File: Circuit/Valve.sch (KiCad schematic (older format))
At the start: 22 parts, among them CN1 GROVE, CN2 ST-LINK, CN3 TTL-232R-3V3, J1 Conn_01x04_Male, SW1 RESET, U1 STM32L010F4P6

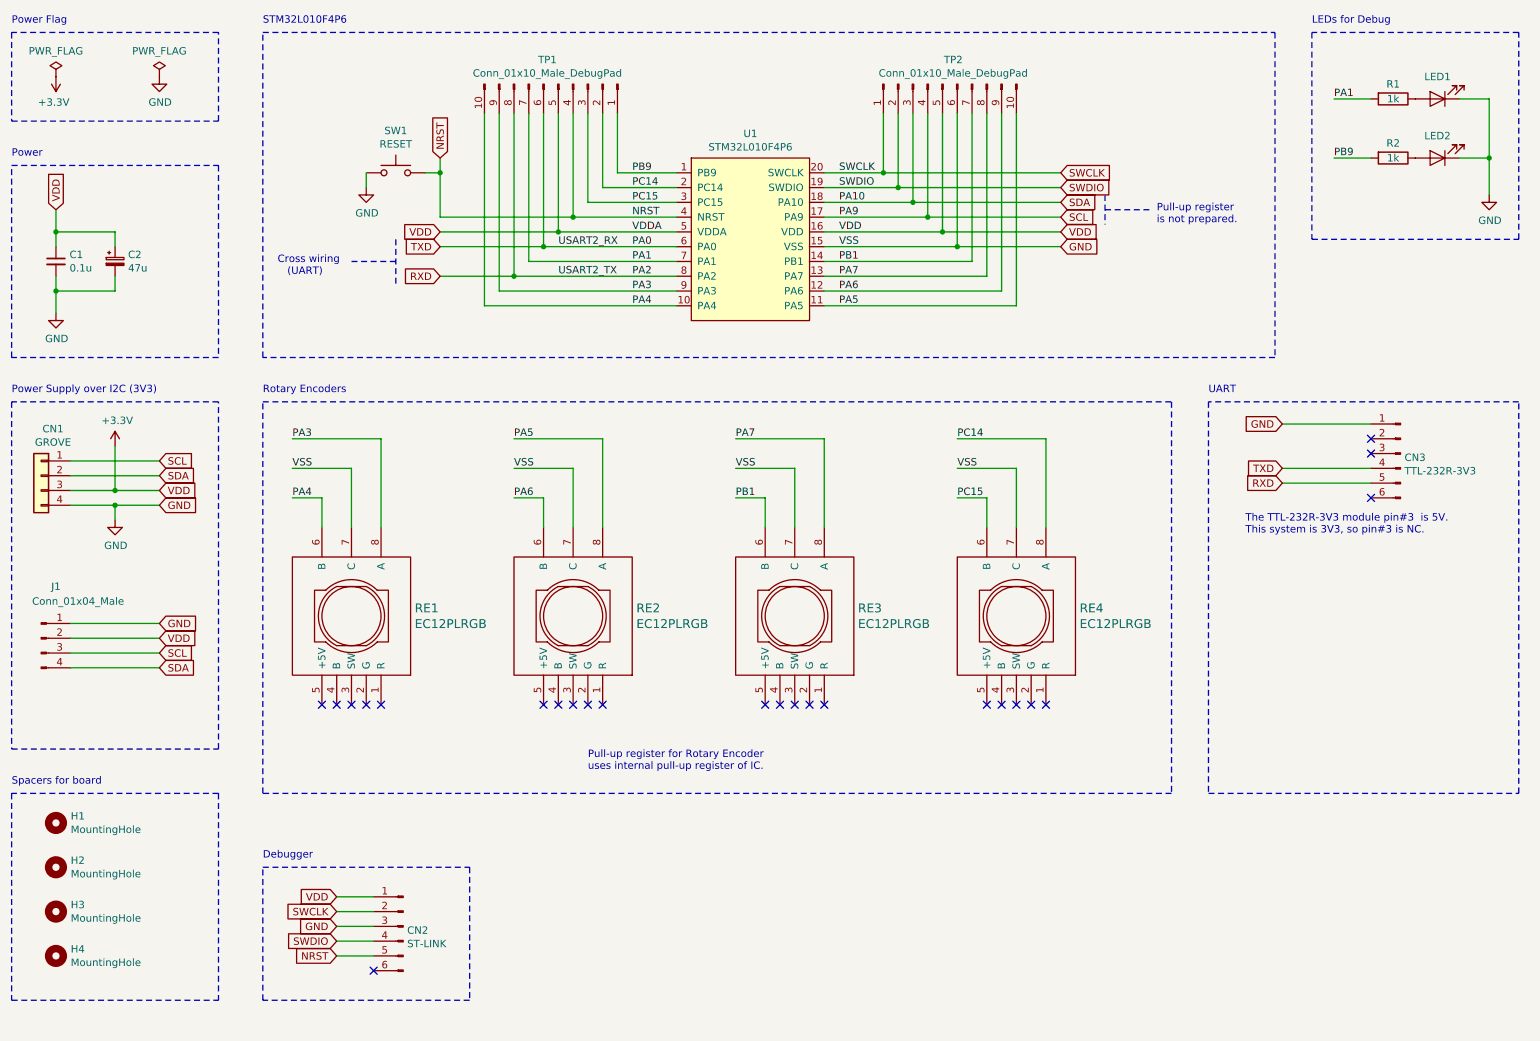
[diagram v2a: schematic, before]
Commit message: I2C プルアップ抵抗 (DNP) を追加
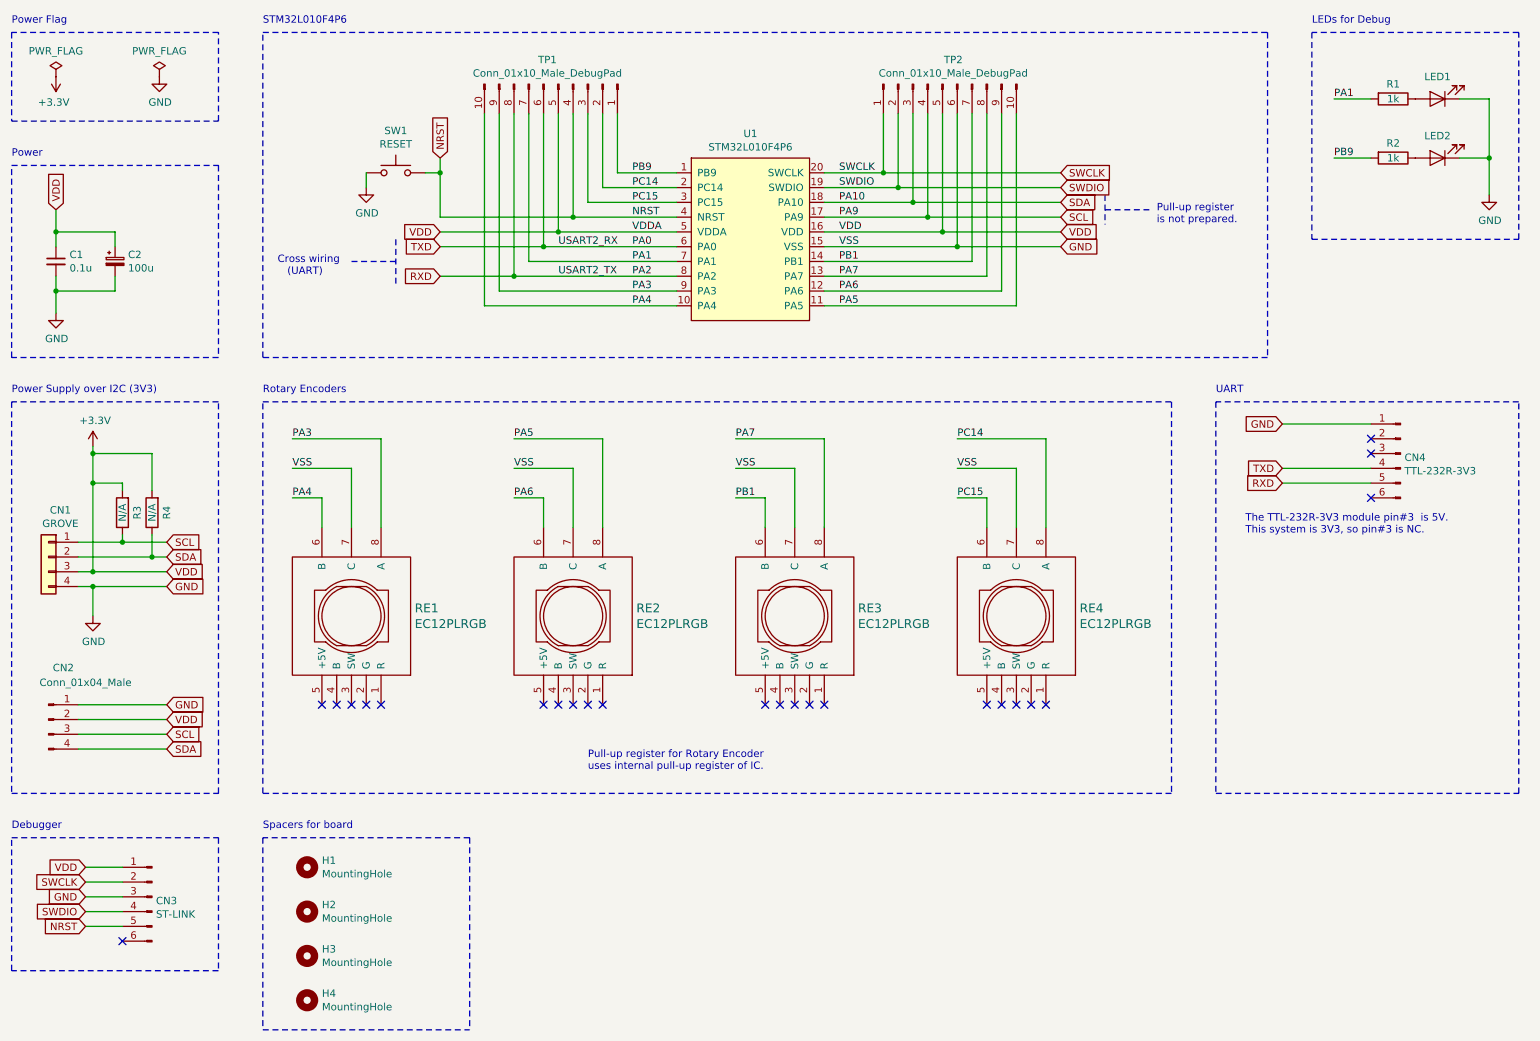
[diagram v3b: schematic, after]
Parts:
- added R3, R4: N/A, Resistor_THT:R_Axial_DIN0207_L6.3mm_D2.5mm_P7.62mm_Horizontal, symbol Device:R
- C2: value 47u -> 100u; footprint Capacitor_THT:CP_Radial_D5.0mm_P2.50mm -> Capacitor_THT:CP_Radial_D6.3mm_P2.50mm
- renumbered J1 to CN2, CN2 to CN3, CN3 to CN4
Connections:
- net +3V3: now also R3.2, R4.2
- net SCL: now also R3.1
- net SDA: now also R4.1
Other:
- moved on the sheet: CN1, CN2, CN3, H1, H2, H3, H4
